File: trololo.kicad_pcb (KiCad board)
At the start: 4 copper layers, 136 x 54.8 mm, 96 parts, among them J1 USB_OTG, J10 Conn_02x12_Odd_Even, J11 Conn_02x02_Odd_Even, J12 PROTO1, J13 PROTO1, J14 PROTO1, J15 PROTO1, J16 PROTO1, J17 PROTO1, J18 PROTO1, J19 PROTO1, J2 USB_OTG, J3 Wuerth_7499010121A, J4 Micro_SD_Card, J5 Screw_Terminal_01x06, J6 Conn_02x12_Odd_Even, J7 USB_OTG, J8 Screw_Terminal_01x02, J9 Conn_02x12_Odd_Even, SW1 RESET, SW2 RESET, U1 STM32H743VITx, U10 USBLC6-2SC6, U2 KSZ8081RNA, U3 TCAN332DCNR, U4 ST485EBDR, U5 W25Q32JVZP, U6 APE1707H-33-HF, U7 USBLC6-2SC6, U8 STM32F042G6Ux, U9 USBLC6-2SC6, Y1 8MHz, Y2 32.768KHz, Y3 25MHz

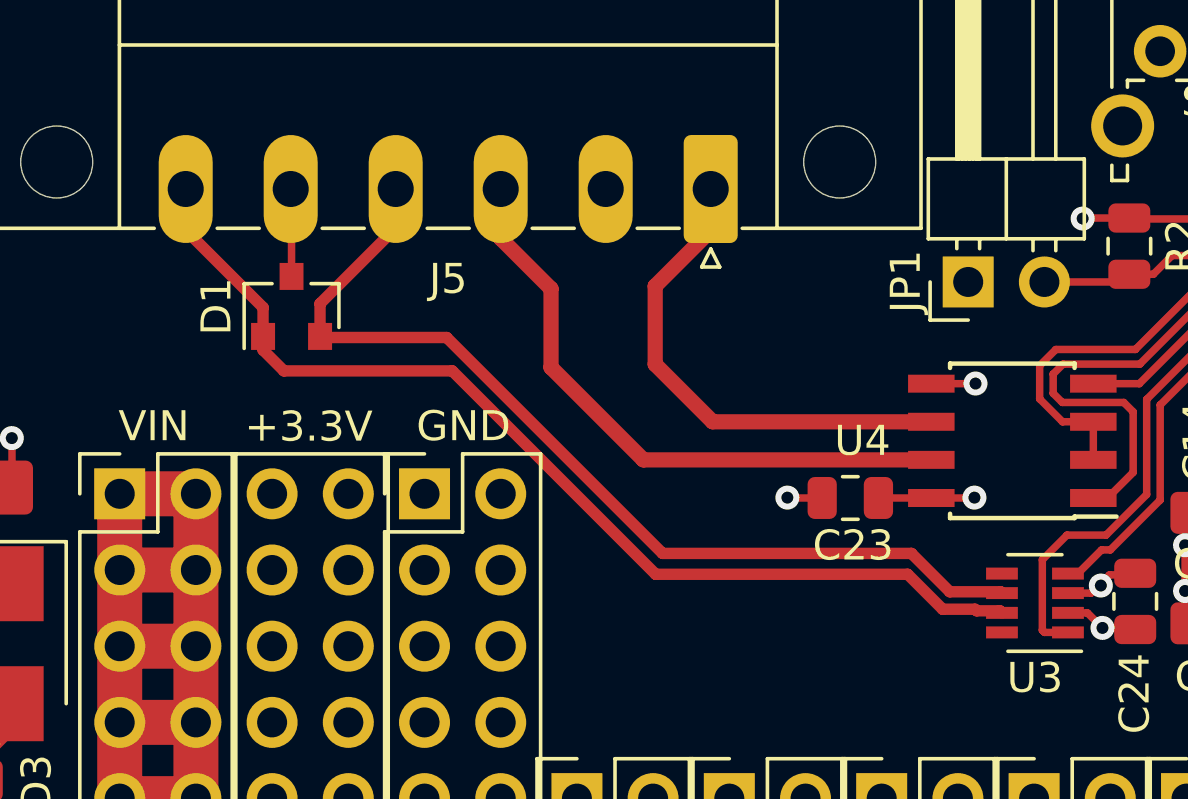
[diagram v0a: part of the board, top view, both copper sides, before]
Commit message: Final aproach with no can/485 isolation
Signed-off-by: Martin Ribelotta <martinribelotta@gmail.com>
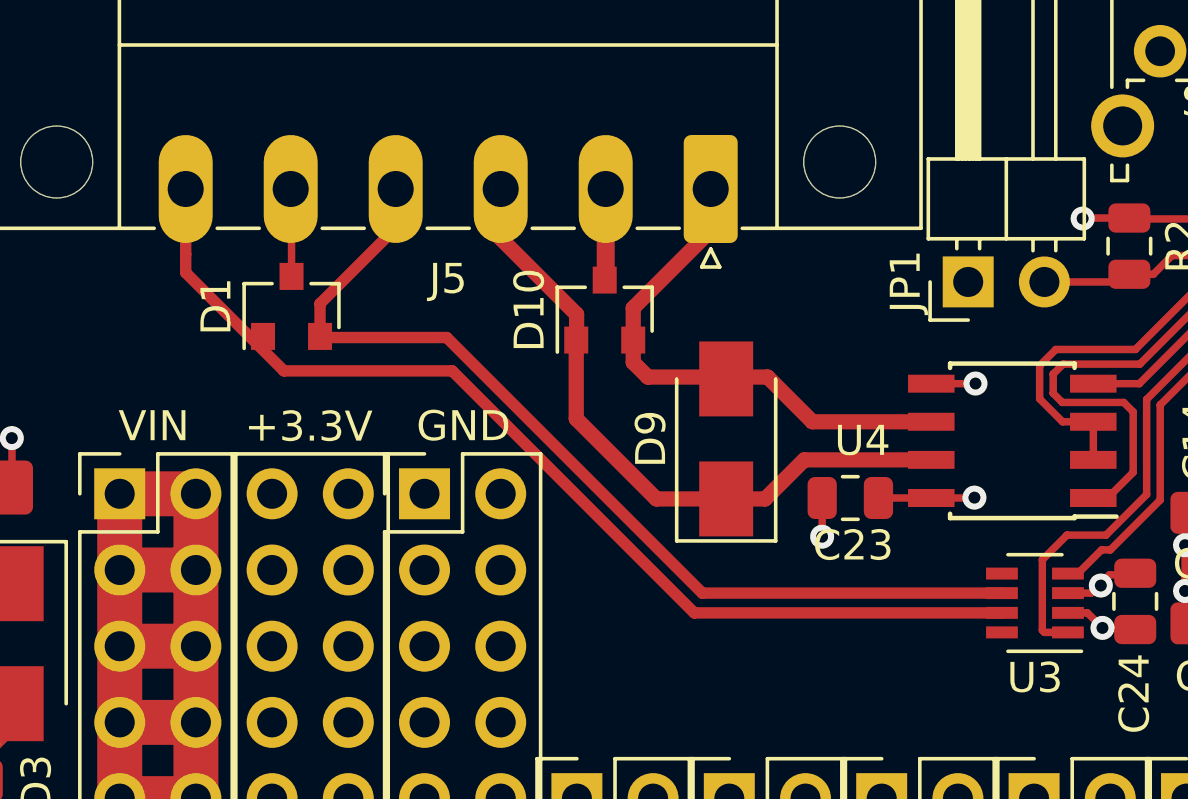
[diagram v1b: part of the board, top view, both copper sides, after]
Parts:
- added D10: NUP2105L, Package_TO_SOT_SMD:SOT-23, F.Cu at (89.8, 39.6)
- added D9: D_TVS, Diode_SMD:D_SMA, F.Cu at (93.9, 43.9)
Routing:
- net GND: track 158.7 -> 161.9 mm
- net /RS485_B: track 20.6 -> 22.2 mm
- net /RS485_A: track 16.6 -> 17.6 mm

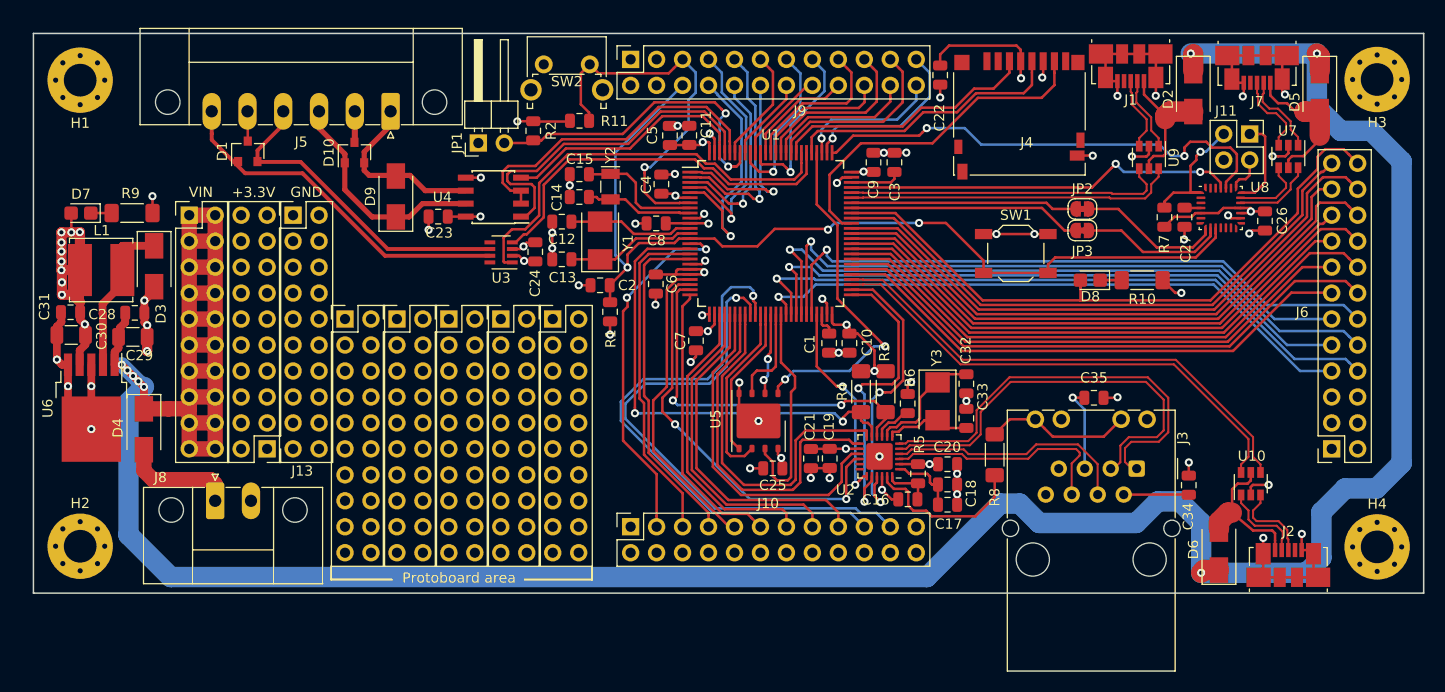
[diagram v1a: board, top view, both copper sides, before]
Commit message: First isolation aproach
Signed-off-by: Martin Ribelotta <martinribelotta@gmail.com>
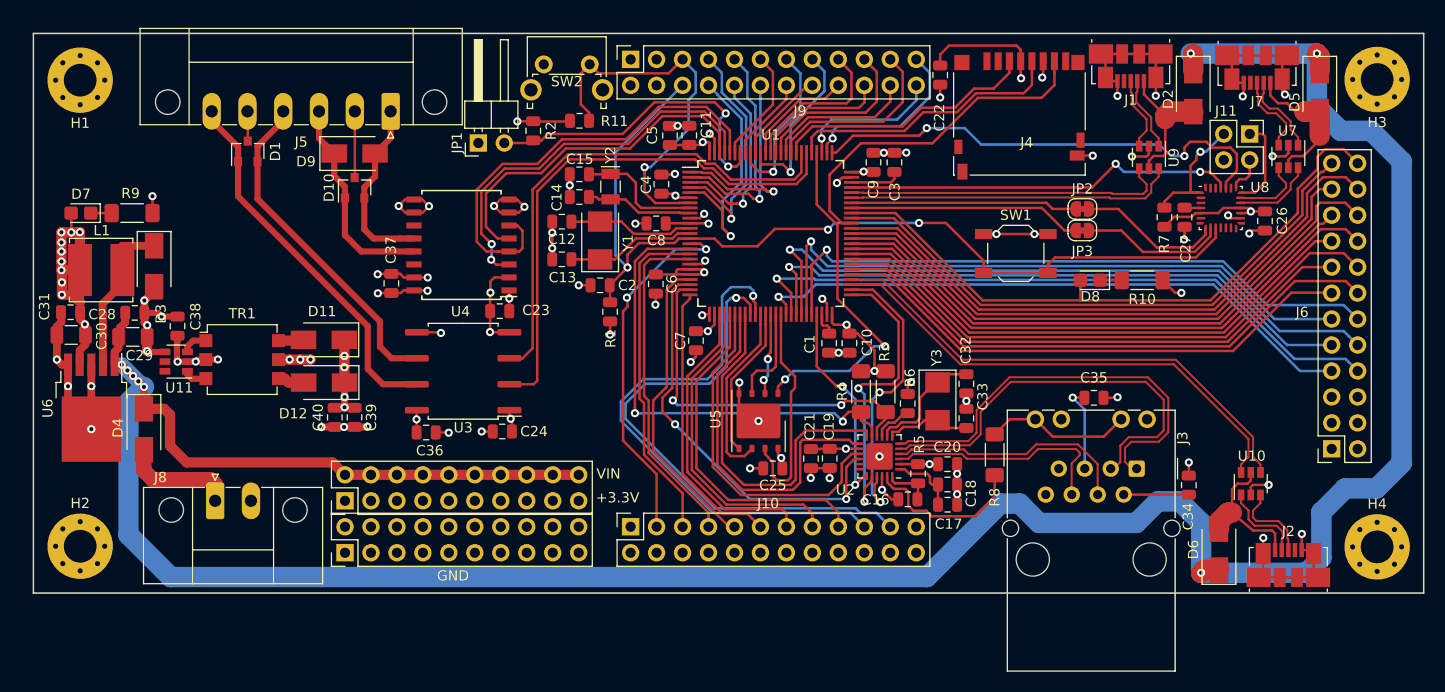
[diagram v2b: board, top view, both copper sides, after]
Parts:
- removed J12, J14, J15, J16, J17, J19: PROTO1, Connector_PinHeader_2.54mm:PinHeader_2x10_P2.54mm_Vertical
- added C36: 0.1u, Capacitor_SMD:C_0805_2012Metric, F.Cu at (96.8, 67.0)
- added C37: 0.1u, Capacitor_SMD:C_0805_2012Metric, F.Cu at (93.4, 52.4)
- added C38: 0.1u, Capacitor_SMD:C_0805_2012Metric, F.Cu at (72.5, 56.6)
- added C39: 10u, Capacitor_SMD:C_0805_2012Metric, F.Cu at (89.8, 65.5)
- added C40: 0.1u, Capacitor_SMD:C_0805_2012Metric, F.Cu at (87.9, 65.5)
- added D11: B120-E3, Diode_SMD:D_SMA, F.Cu at (86.8, 57.9)
- added D12: B120-E3, Diode_SMD:D_SMA, F.Cu at (86.9, 62.1)
- added TR1: ADTT1-6, Transformer_SMD:Pulse_P0926NL, F.Cu at (78.8, 59.8)
- added U11: SN6505, Package_TO_SOT_SMD:SOT-23-6, F.Cu at (72.4, 60.0)
- U3: value TCAN332DCNR -> ISO1050DUB; footprint Package_TO_SOT_SMD:SOT-23-8 -> Package_SO:SOP-8_6.62x9.15mm_P2.54mm
- U4: value ST485EBDR -> ISO3082DW; footprint Package_SO:SOIC-8_3.9x4.9mm_P1.27mm -> Package_SO:SOIC-16W_7.5x10.3mm_P1.27mm
- moved J13 33.4 mm to (88.9, 78.7), turned to 90 degrees
- moved C24 17.9 mm to (104.3, 66.9), turned to 0 degrees
- moved U3 12.2 mm to (100.5, 61.0)
- moved C23 11.0 mm to (104.0, 55.1)
- moved J18 9.16 mm to (88.9, 73.7), turned to 90 degrees
- moved D9 5.83 mm to (89.8, 39.7), turned to 0 degrees
- moved U4 5.62 mm to (100.3, 48.6)
- moved D10 3.44 mm to (89.8, 43.0)
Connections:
- D1 pad 3: GND -> GNDPWR
- D10 pad 3: GND -> GNDPWR
- J18 pad 10: +3V3 -> VDC
- J18 pad 12: +3V3 -> VDC
- J18 pad 14: +3V3 -> VDC
- J18 pad 16: +3V3 -> VDC
- J18 pad 18: +3V3 -> VDC
- J18 pad 2: +3V3 -> VDC
- J18 pad 20: +3V3 -> VDC
- J18 pad 4: +3V3 -> VDC
- J18 pad 6: +3V3 -> VDC
- J18 pad 8: +3V3 -> VDC
- J5 pad 2: GND -> GNDPWR
- J5 pad 5: GND -> GNDPWR
- U3 pad 1: /CAN_TX -> +3V3
- U3 pad 2: GND -> /CAN_RX
- U3 pad 3: +3V3 -> /CAN_TX
- U3 pad 4: /CAN_RX -> GND
- U3 pad 5: Net-(U3-Pad5) -> GNDPWR
- U3 pad 8: Net-(U3-Pad8) -> +5P
- U4 pad 1: /RS485_RX -> +3V3
- U4 pad 2: /RS485_DE -> GND
- U4 pad 3: /RS485_DE -> /RS485_RX
- U4 pad 4: /RS485_TX -> /RS485_DE
- U4 pad 5: GND -> /RS485_TX
- U4 pad 6: /RS485_A -> /RS485_DE
- U4 pad 7: /RS485_B -> GND
- U4 pad 8: +3V3 -> GND
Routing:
- net GNDPWR: track 0.00 -> 32.8 mm, vias 0 -> 12
- net VDC: track 311.7 -> 283.1 mm
- net +5P: track 0.00 -> 15.8 mm, vias 0 -> 7
- net /CAN_RX: track 37.5 -> 52.5 mm
- net /RS485_DE: track 32.5 -> 44.6 mm
- net GND: track 161.9 -> 172.8 mm, vias 60 -> 63
- net /RS485_TX: track 24.5 -> 34.6 mm
- net /CAN_TX: track 40.8 -> 49.2 mm
- net +3V3: track 111.0 -> 116.1 mm, vias 27 -> 30
- net /RS485_RX: track 33.9 -> 39.0 mm, vias 0 -> 2
- net Net-(D12-Pad2): track 0.00 -> 2.62 mm
- net Net-(TR1-Pad1): track 0.00 -> 2.58 mm
- net Net-(D11-Pad2): track 0.00 -> 2.47 mm
- net Net-(TR1-Pad3): track 0.00 -> 2.31 mm
- net /CAN_H: track 34.7 -> 37.0 mm
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- added copper zone on In2.Cu, net +5P
- added copper zone on In1.Cu, net GNDPWR
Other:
- board text removed: "Protoboard area"

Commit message: Unknown changes
Signed-off-by: Martin Ribelotta <martinribelotta@gmail.com>
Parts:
- removed D3: D_Schottky_Small_ALT, Diode_SMD:D_SMA
- removed D9: D_TVS, Diode_SMD:D_SMA
- added JP4: Jumper_2_Bridged, Jumper:SolderJumper-2_P1.3mm_Open_RoundedPad1.0x1.5mm, F.Cu at (100.2, 42.8)
- added JP5: Jumper_2_Bridged, Jumper:SolderJumper-2_P1.3mm_Open_RoundedPad1.0x1.5mm, F.Cu at (117.8, 42.4)
- added U12: TCAN332, Package_TO_SOT_SMD:SOT-23-8, F.Cu at (100.4, 59.6)
- added U13: ISL83483, Package_SO:SOIC-8_3.9x4.9mm_P1.27mm, F.Cu at (100.1, 46.6)
- C29: value 470u -> 10u; footprint Capacitor_SMD:C_1206_3216Metric -> Capacitor_SMD:C_0805_2012Metric
- C30: value 470u -> 2.2u; footprint Capacitor_SMD:C_1206_3216Metric -> Capacitor_SMD:C_0805_2012Metric
- C31: value 0.1u -> 2.2u
- J1, J2, J7: value USB_OTG -> 10118194-0001LF; footprint Connector_USB:USB_Micro-B_Molex_47346-0001 -> footprints:USB_Micro_B_Female_10118194-0001LF
- J10, J6, J9: moved to B.Cu
- J3: value Wuerth_7499010121A -> RJ45_Amphenol_RJMG1BD3B8K1ANR; footprint Connector_RJ:RJ45_Wuerth_7499010121A_Horizontal -> Connector_RJ:RJ45_Amphenol_RJMG1BD3B8K1ANR
- L1: value L_Small -> 68uH; footprint Inductor_SMD:L_Bourns_SRN6045TA -> Inductor_SMD:L_6.3x6.3_H3
- R10, R3, R4, R8, R9: footprint Resistor_SMD:R_1806_4516Metric -> Resistor_SMD:R_0805_2012Metric
- SW2: value RESET -> PC13
- U5: value W25Q32JVZP -> S25FL127SABMFI101; footprint Package_SON:WSON-8-1EP_6x5mm_P1.27mm_EP3.4x4.3mm -> footprints:S25FL127SABMFI101
- U6: value APE1707H-33-HF -> AP63203; footprint Package_TO_SOT_SMD:TO-252-5_TabPin3 -> Package_TO_SOT_SMD:TSOT-23-6
- U8: value STM32F042G6Ux -> STM32F042F6Px; footprint Package_DFN_QFN:QFN-28_4x4mm_P0.5mm -> Package_SO:TSSOP-20_4.4x6.5mm_P0.65mm
- moved J6 27.9 mm to (185.4, 40.6)
- moved C39 15.3 mm to (81.9, 52.3), turned to 90 degrees
- moved C40 13.8 mm to (83.9, 52.3), turned to 90 degrees
- moved C22 12.9 mm to (154.6, 42.5), turned to 0 degrees
- moved C31 12.8 mm to (68.7, 66.1)
- moved C34 12.7 mm to (165.7, 60.8), turned to 180 degrees
- moved C29 12.0 mm to (67.8, 69.7), turned to 90 degrees
- moved C28 11.6 mm to (61.7, 64.8), turned to 90 degrees
- moved D4 9.29 mm to (78.2, 68.9), turned to 180 degrees
- moved C35 9.17 mm to (170.9, 60.8), turned to 0 degrees
- moved C30 8.86 mm to (68.8, 63.3)
- moved R8 8.27 mm to (147.9, 76.1), turned to 180 degrees
- moved U10 8.23 mm to (180.0, 64.2)
- moved R9 8.06 mm to (60.6, 48.4), turned to 270 degrees
- moved L1 7.92 mm to (62.6, 58.6), turned to 90 degrees
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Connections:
- C28 pad 1: VDC -> Net-(C28-Pad1)
- C28 pad 2: GND -> Net-(C28-Pad2)
- C4 pad 1: +3V3 -> +BATT
- J10 pad 10: GND -> /PA0
- J10 pad 11: /PA3 -> GND
- J10 pad 12: GND -> /PA3
- J10 pad 13: /PA4 -> GND
- J10 pad 14: GND -> /PA4
- J10 pad 15: /PA5 -> GND
- J10 pad 16: GND -> /PA5
- J10 pad 17: /PA6 -> GND
- J10 pad 18: GND -> /PA6
- J10 pad 19: /PB1 -> GND
- J10 pad 20: GND -> /PB1
- J10 pad 21: /PB0 -> GND
- J10 pad 22: GND -> /PB0
- J10 pad 3: /PC0 -> GND
- J10 pad 4: GND -> /PC0
- J10 pad 5: /PC2 -> GND
- J10 pad 6: GND -> /PC2
- J10 pad 7: /PC3 -> GND
- J10 pad 8: GND -> /PC3
- J10 pad 9: /PA0 -> GND
- J13 pad 1: GND -> +3V3
- J13 pad 11: GND -> +3V3
- J13 pad 13: GND -> +3V3
- J13 pad 15: GND -> +3V3
- J13 pad 17: GND -> +3V3
- J13 pad 19: GND -> +3V3
- J13 pad 3: GND -> +3V3
- J13 pad 5: GND -> +3V3
- J13 pad 7: GND -> +3V3
- J13 pad 9: GND -> +3V3
- J18 pad 1: +3V3 -> GND
- J18 pad 11: +3V3 -> GND
- J18 pad 13: +3V3 -> GND
- J18 pad 15: +3V3 -> GND
- J18 pad 17: +3V3 -> GND
- J18 pad 19: +3V3 -> GND
- J18 pad 3: +3V3 -> GND
- J18 pad 5: +3V3 -> GND
- J18 pad 7: +3V3 -> GND
- J18 pad 9: +3V3 -> GND
- J6 pad 1: GND -> /PC9
- J6 pad 10: /PE14 -> /PD11
- J6 pad 11: /PE15 -> /PD8
- J6 pad 12: /PB10 -> /PD9
- J6 pad 13: /PD8 -> /PE15
- J6 pad 14: /PD9 -> /PB10
- J6 pad 15: /PD10 -> /PE13
- J6 pad 16: /PD11 -> /PE14
- J6 pad 17: /PD12 -> /PE11
- J6 pad 18: /PD13 -> /PE12
- J6 pad 19: /PD14 -> /U1_RX
- J6 pad 2: +3V3 -> /PA8
- J6 pad 20: /PD15 -> /U1_TX
- J6 pad 21: /PC6 -> GND
- J6 pad 22: /PC7 -> +3V3
- J6 pad 23: /PC9 -> GND
- J6 pad 24: /PA8 -> +3V3
- J6 pad 3: GND -> /PC6
- J6 pad 4: +3V3 -> /PC7
- J6 pad 5: GND -> /PD14
- J6 pad 6: +3V3 -> /PD15
- J6 pad 7: /PE11 -> /PD12
- J6 pad 8: /PE12 -> /PD13
- J6 pad 9: /PE13 -> /PD10
- J9 pad 1: +3V3 -> GND
- J9 pad 10: /PE4 -> /PE3
- J9 pad 11: /PB8 -> /PE2
- J9 pad 12: /PE2 -> /PB8
- J9 pad 13: /PB6 -> /PB7
- J9 pad 14: /PB7 -> /PB6
- J9 pad 15: /PB4 -> /PB5
- J9 pad 16: /PB5 -> /PB4
- J9 pad 17: /PD7 -> /PB3
- J9 pad 18: /PB3 -> /PD7
- J9 pad 19: /PD5 -> /PD6
- J9 pad 2: GND -> +3V3
- J9 pad 20: /PD6 -> /PD5
- J9 pad 21: /PD3 -> /PD4
- J9 pad 22: /PD4 -> /PD3
- J9 pad 23: /PA15 -> /PC10
- J9 pad 24: /PC10 -> /PA15
- J9 pad 3: +3V3 -> +BATT
- J9 pad 4: GND -> +3V3
- J9 pad 5: /PC13 -> /~RESET
- J9 pad 6: /~RESET -> /PC13
- J9 pad 7: /PE5 -> /PE6
- J9 pad 8: /PE6 -> /PE5
- J9 pad 9: /PE3 -> /PE4
- L1 pad 1: Net-(D3-Pad1) -> Net-(C28-Pad2)
- R8 pad 1: Net-(J3-Pad10) -> Net-(J3-PadL1)
- U1 pad 6: +3V3 -> +BATT
- U11 pad 5: Net-(U11-Pad5) -> +3V3
- U6 pad 1: VDC -> +3V3
- U6 pad 2: Net-(D3-Pad1) -> VDC
- U6 pad 3: GND -> VDC
- U6 pad 4: +3V3 -> GND
- U6 pad 5: GND -> Net-(C28-Pad2)
- U8 pad 15: Net-(U8-Pad15) -> GND
- U8 pad 16: GND -> +3V3
- U8 pad 17: +3V3 -> /USB_SER_D-
- U8 pad 18: +3V3 -> /USB_SER_D+
- U8 pad 19: /USB_SER_D- -> /SWDIO_B
- U8 pad 20: /USB_SER_D+ -> /SWCLK_B
- U8 pad 6: Net-(U8-Pad6) -> /SWCLK
- U8 pad 7: Net-(U8-Pad7) -> /SWDIO
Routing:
- net VDC: track 283.1 -> 224.5 mm, vias 8 -> 22
- net /U1_RX: track 22.2 -> 74.9 mm, vias 0 -> 1
- net +3V3: track 116.1 -> 164.3 mm, vias 30 -> 54
- net /U1_TX: track 22.8 -> 70.4 mm, vias 0 -> 1
- net GND: track 172.8 -> 133.9 mm, vias 63 -> 65
- net Net-(J3-PadL1): track 0.00 -> 25.5 mm, vias 0 -> 1
- net /TD+: track 42.2 -> 22.1 mm, vias 0 -> 1
- net +BATT: track 0.00 -> 18.8 mm, vias 0 -> 1
- net /TD-: track 41.3 -> 22.9 mm, vias 0 -> 1
- net /VBUS2: track 18.0 -> 1.73 mm
- net Net-(D3-Pad1): track 15.6 -> 0.00 mm
- net +5P: track 15.8 -> 30.5 mm, vias 7 -> 11
- net Net-(J3-Pad10): track 14.4 -> 0.00 mm
- net /RD-: track 23.0 -> 36.0 mm, vias 0 -> 1
- net /VBUS3: track 14.2 -> 1.80 mm
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- added copper zone on F.Cu, net +3V3
- added copper zone on F.Cu, net /VBUS1
- added copper zone on F.Cu, net /VBUS2
- added copper zone on F.Cu, net /VBUS3
- added copper zone on F.Cu, net Net-(C28-Pad2)
- added copper zone on B.Cu, net VDC
- added copper zone on F.Cu, net VDC
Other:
- board size 136 x 54.8 mm -> 135.6 x 54.6 mm
- board text added: "5-24V VIN"
- board text added: "A GND B"
- board text added: "BTN PA13"
- board text added: "CANBUS"
- board text added: "Cortex-M7"
- board text added: "DEBUG"
- board text added: "Debug-M0"
- board text added: "H GND L"
- board text added: "ISOLATED AREA"
- board text added: "LED PA8"
- board text added: "MCU RESET"
- board text added: "OTG-1"
- board text added: "OTG-2"
- board text added: "POWER"
- board text added: "RS-485"
- board text added: "STM32H7"

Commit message: More unprecie modifications
The log messages on this git sucks

Signed-off-by: Martin Ribelotta <martinribelotta@gmail.com>
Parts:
- added J12: VBATJ, TestPoint:TestPoint_Loop_D1.80mm_Drill1.0mm_Beaded, F.Cu at (117.7, 42.0)
- JP5: footprint Jumper:SolderJumper-2_P1.3mm_Open_RoundedPad1.0x1.5mm -> Jumper:SolderJumper-2_P1.3mm_Bridged_RoundedPad1.0x1.5mm; moved to B.Cu
- moved JP5 3.09 mm to (117.1, 39.4), turned to 180 degrees
- moved U12 2.20 mm to (100.4, 57.4)
- moved D1 1.18 mm to (79.3, 43.0)
- moved JP4 0.58 mm to (100.4, 42.3)
- moved C4 0.36 mm to (120.2, 42.7)
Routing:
- net +3V3: track 164.3 -> 158.2 mm, vias 54 -> 55
- net /~RESET: track 89.2 -> 83.9 mm
- net /~BOOT: track 31.9 -> 28.2 mm
- net +BATT: track 18.8 -> 15.5 mm, vias 1 -> 0
- net GND: track 133.9 -> 135.3 mm
- net /PE6: track 23.9 -> 25.2 mm
- net /PC13: track 41.1 -> 40.0 mm
- net /PB6: track 16.3 -> 15.2 mm
- net /CAN_RX: track 53.2 -> 54.2 mm
- net /PB4: track 17.2 -> 16.2 mm
- net /CAN_L: track 37.7 -> 36.9 mm
- net /CAN_H: track 41.1 -> 40.3 mm
- net /PB8: track 11.2 -> 10.5 mm
- net /CAN_TX: vias 0 -> 2
